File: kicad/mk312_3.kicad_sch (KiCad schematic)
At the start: 12 parts

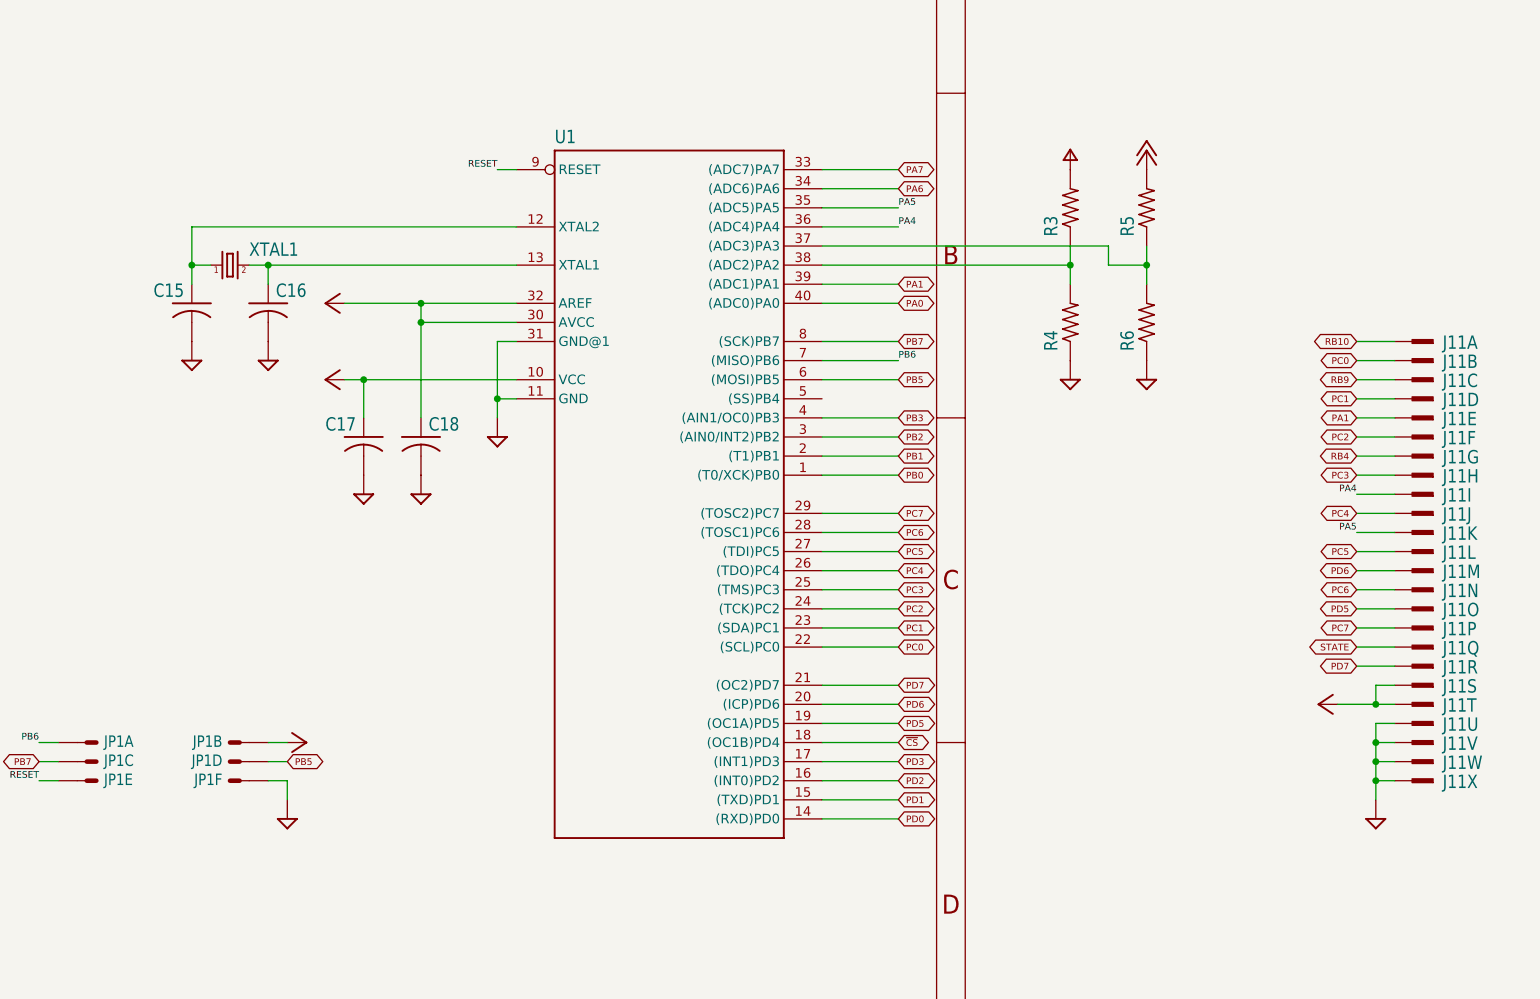
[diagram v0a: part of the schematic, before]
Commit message: Conversion of display print to KiCad components; still attached to main board
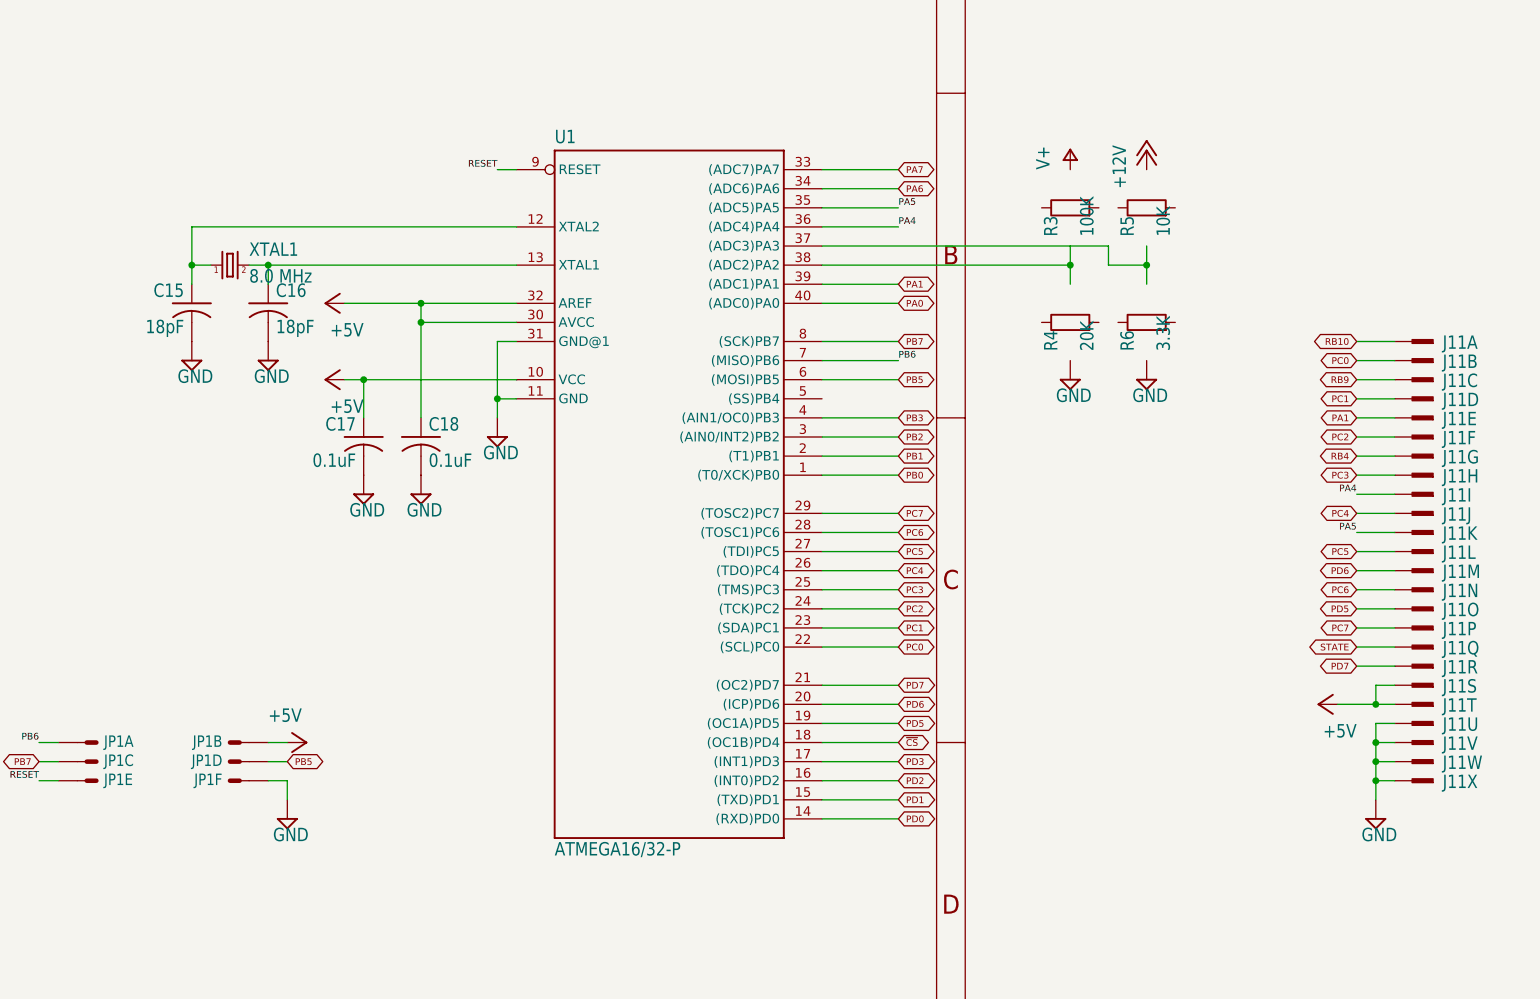
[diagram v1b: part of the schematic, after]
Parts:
- C15, C16: value (none) -> 18pF; footprint (none) -> mk312:C025-024X044
- C17, C18: value (none) -> 0.1uF; footprint (none) -> mk312:C025-024X044
- J11: value (none) -> FRONT PANEL; footprint (none) -> mk312:PAK100_2500-24
- JP1: value (none) -> ISP; footprint (none) -> mk312:057-006-1
- R3: value (none) -> 100K; footprint (none) -> mk312:0207_10; symbol mk312-eagle-import:R-US_0207/10 -> Device:R
- R4: value (none) -> 20K; footprint (none) -> mk312:0207_10; symbol mk312-eagle-import:R-US_0207/10 -> Device:R
- R5: value (none) -> 10K; footprint (none) -> mk312:0207_10; symbol mk312-eagle-import:R-US_0207/10 -> Device:R
- R6: value (none) -> 3.3K; footprint (none) -> mk312:0207_10; symbol mk312-eagle-import:R-US_0207/10 -> Device:R
- U1: value (none) -> ATMEGA16/32-P; footprint (none) -> mk312:DIL40
- XTAL1: value (none) -> 8.0 MHz; footprint (none) -> mk312:HC49_S
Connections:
- net +12V: no longer R5.2
- net GND: no longer R4.1, R6.1
- net V+: no longer R3.2
- now unconnected: R3.1, R4.2, R5.1, R6.2, U1.37 ((ADC3)PA3), U1.38 ((ADC2)PA2)
